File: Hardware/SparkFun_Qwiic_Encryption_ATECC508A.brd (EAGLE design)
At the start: 25.4 x 25.4 mm, 37 parts, among them J1 QWIIC, J2 QWIIC, J3 PTH, U1 ATECC508A

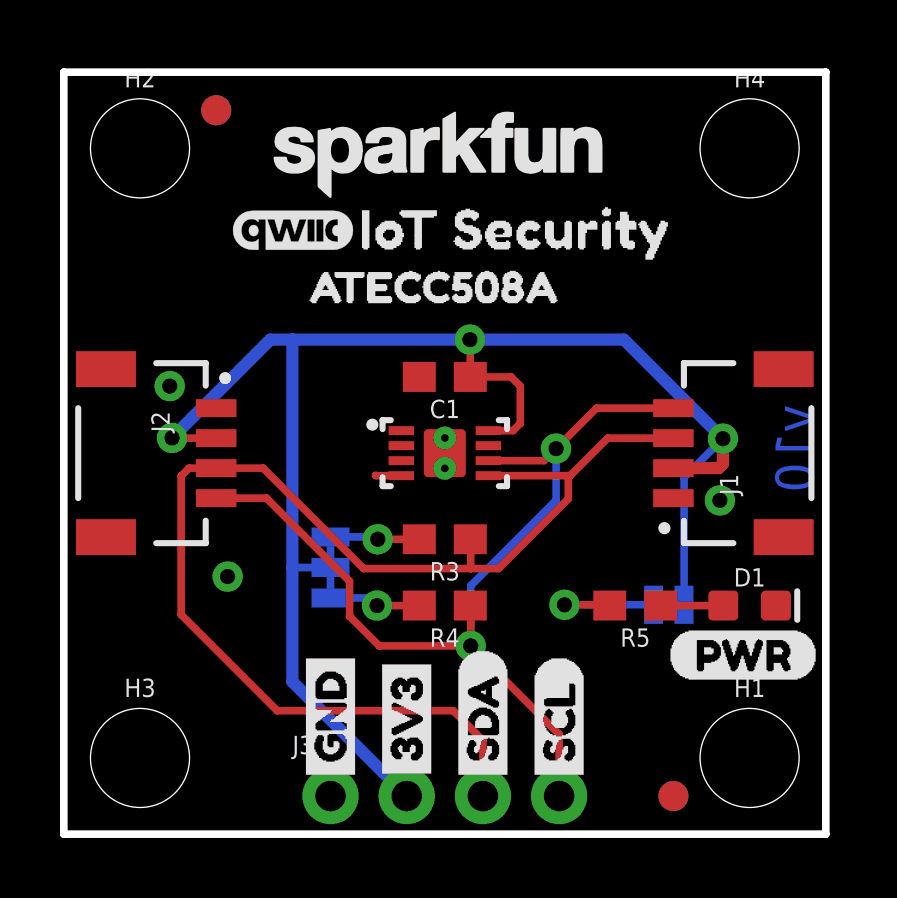
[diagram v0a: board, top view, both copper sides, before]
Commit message: rename and adjusted silk for protos
version to v01
added silk to bplace with name
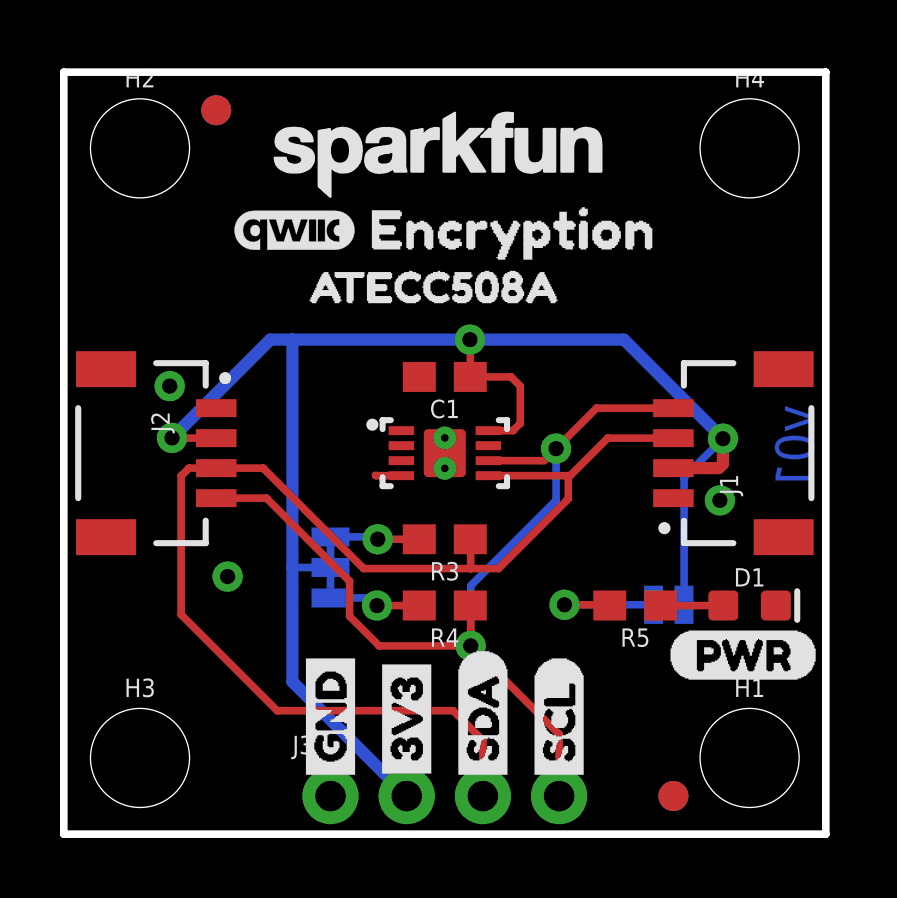
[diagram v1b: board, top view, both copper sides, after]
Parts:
- added U$11: (no value), buzzard_labels (6):ENCRYPTION1
- added U$14: (no value), buzzard_labels (2):ATECC508A0
- added U$9: (no value), SparkFun-Aesthetics:QWIIC_4MM
- U$15: device buzzard_labels (5):IOT_SECURITY0 -> buzzard_labels (6):ENCRYPTION1
- moved U$15 6.91 mm to (15.6, 20.2), flipped to the bottom
- moved LOGO4 4.36 mm to (12.5, 15.7)
- moved U$16 0.05 mm to (7.70, 20.1)
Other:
- board text added: "v01"
- board text removed: "v10"
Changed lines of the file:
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@@
 <grid distance="0.05" unitdist="inch" unit="inch" style="lines" multiple="1" display="yes" altdistance="0.001" altunitdist="inch" altunit="inch"/>
 <layers>
-<layer number="1" name="Top" color="4" fill="1" visible="no" active="yes"/>
+<layer number="1" name="Top" color="4" fill="1" visible="yes" active="yes"/>
 <layer number="16" name="Bottom" color="1" fill="1" visible="yes" active="yes"/>
 <layer number="17" name="Pads" color="2" fill="1" visible="yes" active="yes"/>
@@
 <layer number="28" name="bValues" color="7" fill="1" visible="no" active="yes"/>
 <layer number="29" name="tStop" color="7" fill="3" visible="no" active="yes"/>
-<layer number="30" name="bStop" color="7" fill="6" visible="yes" active="yes"/>
+<layer number="30" name="bStop" color="7" fill="6" visible="no" active="yes"/>
 <layer number="31" name="tCream" color="7" fill="4" visible="no" active="yes"/>
 <layer number="32" name="bCream" color="7" fill="5" visible="no" active="yes"/>
@@
 <wire x1="25.4" y1="25.4" x2="25.4" y2="0" width="0.254" layer="20"/>
 <wire x1="25.4" y1="0" x2="0" y2="0" width="0.254" layer="20"/>
-<text x="24.3586" y="12.8524" size="1.27" layer="16" font="vector" ratio="24" rot="SMR270" align="center">v10</text>
+<text x="24.3586" y="12.8524" size="1.27" layer="16" font="vector" ratio="24" rot="SMR270" align="center">v01</text>
 <text x="16.51" y="-12.7" size="1.778" layer="51" font="vector">Pete Lewis</text>
 <dimension x1="0" y1="0" x2="0" y2="25.4" x3="-10.16" y3="12.7" textsize="1.778" layer="47" unit="inch" visible="yes"/>
@@
 <attribute name="VALUE" x="7.747" y="8.89" size="0.6096" layer="28" font="vector" ratio="20" rot="MR90" align="top-center"/>
 </element>
-<element name="LOGO4" library="SparkFun-Aesthetics" package="OSHW-LOGO-S" value="OSHW-LOGOS" x="12.8524" y="20.066" smashed="yes" rot="MR0"/>
+<element name="LOGO4" library="SparkFun-Aesthetics" package="OSHW-LOGO-S" value="OSHW-LOGOS" x="12.4714" y="15.7226" smashed="yes" rot="MR0"/>
 <element name="FD1" library="SparkFun-Aesthetics" package="FIDUCIAL-1X2" value="FIDUCIAL1X2" x="5.08" y="24.13" smashed="yes"/>
 <element name="FD2" library="SparkFun-Aesthetics" package="FIDUCIAL-1X2" value="FIDUCIAL1X2" x="20.32" y="1.27" smashed="yes"/>
@@
 <attribute name="VALUE" x="12.7" y="16.002" size="0.6096" layer="27" font="vector" ratio="20" rot="R180" align="top-center"/>
 </element>
-<element name="U$16" library="SparkFun-Aesthetics" package="QWIIC_4MM" value="" x="7.6454" y="20.1168" smashed="yes"/>
+<element name="U$16" library="SparkFun-Aesthetics" package="QWIIC_4MM" value="" x="7.6962" y="20.1168" smashed="yes"/>
 <element name="D1" library="SparkFun-LED" package="LED-0603" value="RED" x="22.86" y="7.62" smashed="yes">
 <attribute name="NAME" x="22.86" y="8.255" size="0.6096" layer="25" font="vector" ratio="20" align="bottom-center"/>
@@
 <element name="U1" library="ATECC508A" package="UDFN_2X3MM" value="ATECC508A" x="12.7" y="12.7" smashed="yes" rot="R270"/>
 <element name="U$12" library="buzzard_labels (2)" package="ATECC508A0" value="" x="7.2644" y="18.2372" smashed="yes"/>
-<element name="U$15" library="buzzard_labels (5)" package="IOT_SECURITY0" value="" x="8.7376" y="20.1676" smashed="yes"/>
+<element name="U$11" library="buzzard_labels (6)" package="ENCRYPTION1" value="" x="9.0678" y="20.1676" smashed="yes"/>
+<element name="U$9" library="SparkFun-Aesthetics" package="QWIIC_4MM" value="" x="17.018" y="20.1676" smashed="yes" rot="MR0"/>
+<element name="U$14" library="buzzard_labels (2)" package="ATECC508A0" value="" x="17.4498" y="18.288" smashed="yes" rot="MR0"/>
+<element name="U$15" library="buzzard_labels (6)" package="ENCRYPTION1" value="" x="15.6464" y="20.2184" smashed="yes" rot="MR0"/>
 </elements>
 <signals>

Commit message: Changed silk to correct product name
Also updated sch and board to "v10".
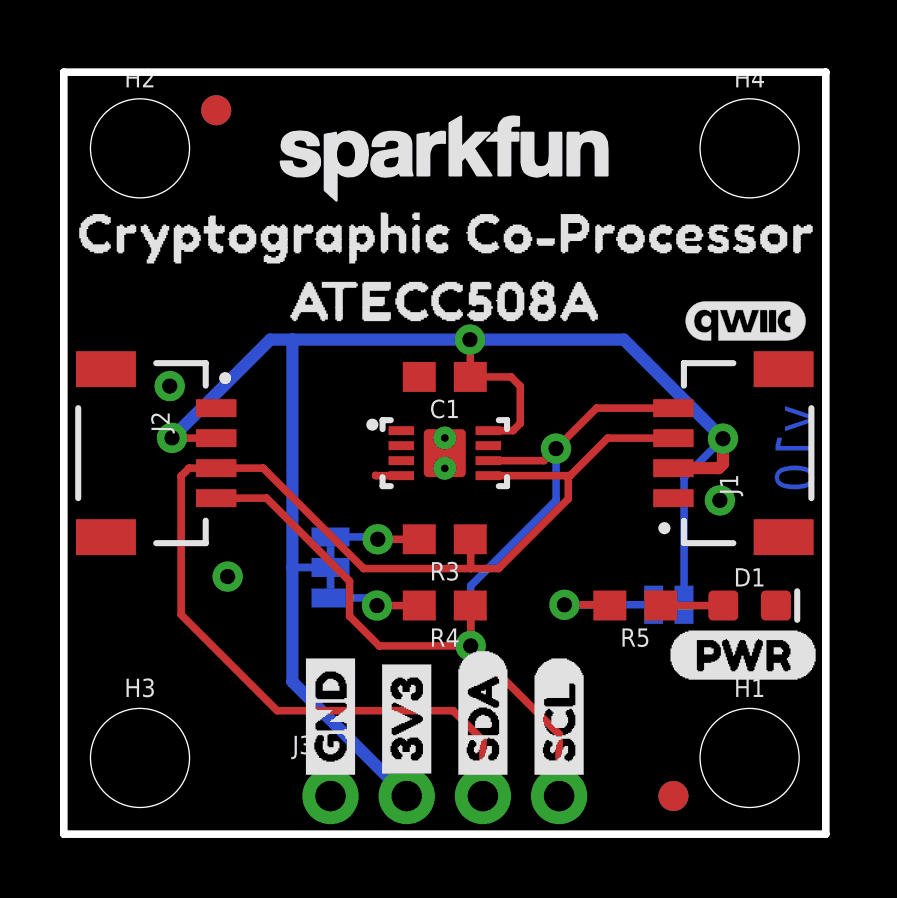
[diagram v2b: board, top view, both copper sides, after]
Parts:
- removed LOGO3: SFE_LOGO_NAME.1_INCH, SparkFun-Aesthetics:SFE_LOGO_NAME_.1@1
- removed U$15: (no value), buzzard_labels (6):ENCRYPTION1
- added LOGO2: SFE_LOGO_NAME.1_INCH, SparkFun-Aesthetics:SFE_LOGO_NAME_.1
- added U$17: (no value), buzzard_labels (5):CRYPTOGRAPHIC_CO#PROCESSOR0
- U$11: device buzzard_labels (6):ENCRYPTION1 -> buzzard_labels (5):CRYPTOGRAPHIC_CO#PROCESSOR0
- U$12, U$14: device buzzard_labels (2):ATECC508A0 -> buzzard_labels (7):ATECC508A0
- moved U$11 16.9 mm to (26.0, 20.0), flipped to the bottom
- moved U$16 15.3 mm to (22.7, 17.1)
- moved U$9 6.31 mm to (12.7, 15.5)
- moved LOGO4 3.03 mm to (12.7, 12.7)
- moved U$14 1.63 mm to (19.0, 17.8)
- moved U$12 1.02 mm to (6.35, 17.8)
- moved LOGO1 0.24 mm to (12.7, 22.5)
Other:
- board text added: "v10"
- board text removed: "v01"
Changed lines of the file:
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@@
 <layer number="23" name="tOrigins" color="15" fill="1" visible="yes" active="yes"/>
 <layer number="24" name="bOrigins" color="15" fill="1" visible="yes" active="yes"/>
-<layer number="25" name="tNames" color="7" fill="1" visible="no" active="yes"/>
-<layer number="26" name="bNames" color="7" fill="1" visible="no" active="yes"/>
-<layer number="27" name="tValues" color="7" fill="1" visible="no" active="yes"/>
-<layer number="28" name="bValues" color="7" fill="1" visible="no" active="yes"/>
-<layer number="29" name="tStop" color="7" fill="3" visible="no" active="yes"/>
-<layer number="30" name="bStop" color="7" fill="6" visible="no" active="yes"/>
-<layer number="31" name="tCream" color="7" fill="4" visible="no" active="yes"/>
-<layer number="32" name="bCream" color="7" fill="5" visible="no" active="yes"/>
-<layer number="33" name="tFinish" color="6" fill="3" visible="no" active="yes"/>
-<layer number="34" name="bFinish" color="6" fill="6" visible="no" active="yes"/>
-<layer number="35" name="tGlue" color="7" fill="4" visible="no" active="yes"/>
-<layer number="36" name="bGlue" color="7" fill="5" visible="no" active="yes"/>
-<layer number="37" name="tTest" color="7" fill="1" visible="no" active="yes"/>
-<layer number="38" name="bTest" color="7" fill="1" visible="no" active="yes"/>
-<layer number="39" name="tKeepout" color="4" fill="11" visible="no" active="yes"/>
-<layer number="40" name="bKeepout" color="1" fill="11" visible="no" active="yes"/>
-<layer number="41" name="tRestrict" color="4" fill="10" visible="no" active="yes"/>
-<layer number="42" name="bRestrict" color="1" fill="10" visible="no" active="yes"/>
-<layer number="43" name="vRestrict" color="2" fill="10" visible="no" active="yes"/>
-<layer number="44" name="Drills" color="7" fill="1" visible="no" active="yes"/>
+<layer number="25" name="tNames" color="7" fill="1" visible="yes" active="yes"/>
+<layer number="26" name="bNames" color="7" fill="1" visible="yes" active="yes"/>
+<layer number="27" name="tValues" color="7" fill="1" visible="yes" active="yes"/>
+<layer number="28" name="bValues" color="7" fill="1" visible="yes" active="yes"/>
+<layer number="29" name="tStop" color="7" fill="3" visible="yes" active="yes"/>
+<layer number="30" name="bStop" color="7" fill="6" visible="yes" active="yes"/>
+<layer number="31" name="tCream" color="7" fill="4" visible="yes" active="yes"/>
+<layer number="32" name="bCream" color="7" fill="5" visible="yes" active="yes"/>
+<layer number="33" name="tFinish" color="6" fill="3" visible="yes" active="yes"/>
+<layer number="34" name="bFinish" color="6" fill="6" visible="yes" active="yes"/>
+<layer number="35" name="tGlue" color="7" fill="4" visible="yes" active="yes"/>
+<layer number="36" name="bGlue" color="7" fill="5" visible="yes" active="yes"/>
+<layer number="37" name="tTest" color="7" fill="1" visible="yes" active="yes"/>
+<layer number="38" name="bTest" color="7" fill="1" visible="yes" active="yes"/>
+<layer number="39" name="tKeepout" color="4" fill="11" visible="yes" active="yes"/>
+<layer number="40" name="bKeepout" color="1" fill="11" visible="yes" active="yes"/>
+<layer number="41" name="tRestrict" color="4" fill="10" visible="yes" active="yes"/>
+<layer number="42" name="bRestrict" color="1" fill="10" visible="yes" active="yes"/>
+<layer number="43" name="vRestrict" color="2" fill="10" visible="yes" active="yes"/>
+<layer number="44" name="Drills" color="7" fill="1" visible="yes" active="yes"/>
 <layer number="45" name="Holes" color="7" fill="1" visible="yes" active="yes"/>
-<layer number="46" name="Milling" color="3" fill="1" visible="no" active="yes"/>
-<layer number="47" name="Measures" color="7" fill="1" visible="no" active="yes"/>
-<layer number="48" name="Document" color="7" fill="1" visible="no" active="yes"/>
+<layer number="46" name="Milling" color="3" fill="1" visible="yes" active="yes"/>
+<layer number="47" name="Measures" color="7" fill="1" visible="yes" active="yes"/>
+<layer number="48" name="Document" color="7" fill="1" visible="yes" active="yes"/>
 <layer number="49" name="Reference" color="13" fill="1" visible="yes" active="yes"/>
-<layer number="50" name="dxf" color="7" fill="1" visible="no" active="yes"/>
+<layer number="50" name="dxf" color="7" fill="1" visible="yes" active="yes"/>
 <layer number="51" name="tDocu" color="6" fill="1" visible="yes" active="yes"/>
-<layer number="52" name="bDocu" color="7" fill="1" visible="no" active="yes"/>
+<layer number="52" name="bDocu" color="7" fill="1" visible="yes" active="yes"/>
 <layer number="91" name="Nets" color="2" fill="1" visible="no" active="no"/>
 <layer number="92" name="Busses" color="1" fill="1" visible="no" active="no"/>
@@
 <wire x1="25.4" y1="25.4" x2="25.4" y2="0" width="0.254" layer="20"/>
 <wire x1="25.4" y1="0" x2="0" y2="0" width="0.254" layer="20"/>
-<text x="24.3586" y="12.8524" size="1.27" layer="16" font="vector" ratio="24" rot="SMR270" align="center">v01</text>
+<text x="24.3586" y="12.8524" size="1.27" layer="16" font="vector" ratio="24" rot="SMR270" align="center">v10</text>
 <text x="16.51" y="-12.7" size="1.778" layer="51" font="vector">Pete Lewis</text>
 <dimension x1="0" y1="0" x2="0" y2="25.4" x3="-10.16" y3="12.7" textsize="1.778" layer="47" unit="inch" visible="yes"/>
@@
 <attribute name="VALUE" x="7.747" y="8.89" size="0.6096" layer="28" font="vector" ratio="20" rot="MR90" align="top-center"/>
 </element>
-<element name="LOGO4" library="SparkFun-Aesthetics" package="OSHW-LOGO-S" value="OSHW-LOGOS" x="12.4714" y="15.7226" smashed="yes" rot="MR0"/>
+<element name="LOGO4" library="SparkFun-Aesthetics" package="OSHW-LOGO-S" value="OSHW-LOGOS" x="12.7" y="12.7" smashed="yes" rot="MR0"/>
 <element name="FD1" library="SparkFun-Aesthetics" package="FIDUCIAL-1X2" value="FIDUCIAL1X2" x="5.08" y="24.13" smashed="yes"/>
 <element name="FD2" library="SparkFun-Aesthetics" package="FIDUCIAL-1X2" value="FIDUCIAL1X2" x="20.32" y="1.27" smashed="yes"/>
@@
 <attribute name="VALUE" x="1.778" y="14.351" size="0.6096" layer="27" font="vector" ratio="20" rot="R270"/>
 </element>
-<element name="LOGO1" library="SparkFun-Aesthetics" package="SFE_LOGO_NAME_.1" value="SFE_LOGO_NAME.1_INCH" x="12.4968" y="22.65045" smashed="yes"/>
+<element name="LOGO1" library="SparkFun-Aesthetics" package="SFE_LOGO_NAME_.1" value="SFE_LOGO_NAME.1_INCH" x="12.7" y="22.52345" smashed="yes"/>
 <element name="FD3" library="SparkFun-Aesthetics" package="FIDUCIAL-1X2" value="FIDUCIAL1X2" x="20.32" y="1.27" smashed="yes" rot="MR0"/>
 <element name="FD4" library="SparkFun-Aesthetics" package="FIDUCIAL-1X2" value="FIDUCIAL1X2" x="5.08" y="24.13" smashed="yes" rot="MR0"/>
-<element name="LOGO3" library="SparkFun-Aesthetics" package="SFE_LOGO_NAME_.1@1" value="SFE_LOGO_NAME.1_INCH" x="18.4912" y="20.79625" smashed="yes" rot="MR0"/>
 <element name="C1" library="SparkFun-Capacitors" package="0603" value="0.1uF" x="12.7" y="15.24" smashed="yes" rot="R180">
 <attribute name="NAME" x="12.7" y="14.478" size="0.6096" layer="25" font="vector" ratio="20" rot="R180" align="bottom-center"/>
@@
 <attribute name="VALUE" x="12.7" y="16.002" size="0.6096" layer="27" font="vector" ratio="20" rot="R180" align="top-center"/>
 </element>
-<element name="U$16" library="SparkFun-Aesthetics" package="QWIIC_4MM" value="" x="7.6962" y="20.1168" smashed="yes"/>
+<element name="U$16" library="SparkFun-Aesthetics" package="QWIIC_4MM" value="" x="22.733" y="17.0942" smashed="yes"/>
 <element name="D1" library="SparkFun-LED" package="LED-0603" value="RED" x="22.86" y="7.62" smashed="yes">
 <attribute name="NAME" x="22.86" y="8.255" size="0.6096" layer="25" font="vector" ratio="20" align="bottom-center"/>
@@
 </element>
 <element name="U1" library="ATECC508A" package="UDFN_2X3MM" value="ATECC508A" x="12.7" y="12.7" smashed="yes" rot="R270"/>
-<element name="U$12" library="buzzard_labels (2)" package="ATECC508A0" value="" x="7.2644" y="18.2372" smashed="yes"/>
-<element name="U$11" library="buzzard_labels (6)" package="ENCRYPTION1" value="" x="9.0678" y="20.1676" smashed="yes"/>
-<element name="U$9" library="SparkFun-Aesthetics" package="QWIIC_4MM" value="" x="17.018" y="20.1676" smashed="yes" rot="MR0"/>
-<element name="U$14" library="buzzard_labels (2)" package="ATECC508A0" value="" x="17.4498" y="18.288" smashed="yes" rot="MR0"/>
-<element name="U$15" library="buzzard_labels (6)" package="ENCRYPTION1" value="" x="15.6464" y="20.2184" smashed="yes" rot="MR0"/>
+<element name="U$9" library="SparkFun-Aesthetics" package="QWIIC_4MM" value="" x="12.7254" y="15.5448" smashed="yes" rot="MR0"/>
+<element name="U$17" library="buzzard_labels (5)" package="CRYPTOGRAPHIC_CO#PROCESSOR0" value="" x="-0.6858" y="20.0406" smashed="yes"/>
+<element name="U$12" library="buzzard_labels (7)" package="ATECC508A0" value="" x="6.35" y="17.78" smashed="yes"/>
+<element name="U$11" library="buzzard_labels (5)" package="CRYPTOGRAPHIC_CO#PROCESSOR0" value="" x="26.0096" y="19.9898" smashed="yes" rot="MR0"/>
+<element name="U$14" library="buzzard_labels (7)" package="ATECC508A0" value="" x="18.9992" y="17.78" smashed="yes" rot="MR0"/>
+<element name="LOGO2" library="SparkFun-Aesthetics" package="SFE_LOGO_NAME_.1" value="SFE_LOGO_NAME.1_INCH" x="12.7" y="22.52345" smashed="yes" rot="MR0"/>
 </elements>
 <signals>
